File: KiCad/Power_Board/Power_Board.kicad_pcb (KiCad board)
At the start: 4 copper layers, 101.6 x 63.5 mm, 271 parts, among them P1 CONN_LEFT_TOP, P10 CONN_02X01, P2 CONN_RIGHT_TOP, P3 CONN_LEFT_BOTTOM, P4 CONN_RIGHT_BOTTOM, P5 CONN_02X01, P6 CONN_02X01, P7 CONN_02X01, P8 CONN_02X01, P9 CONN_02X01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

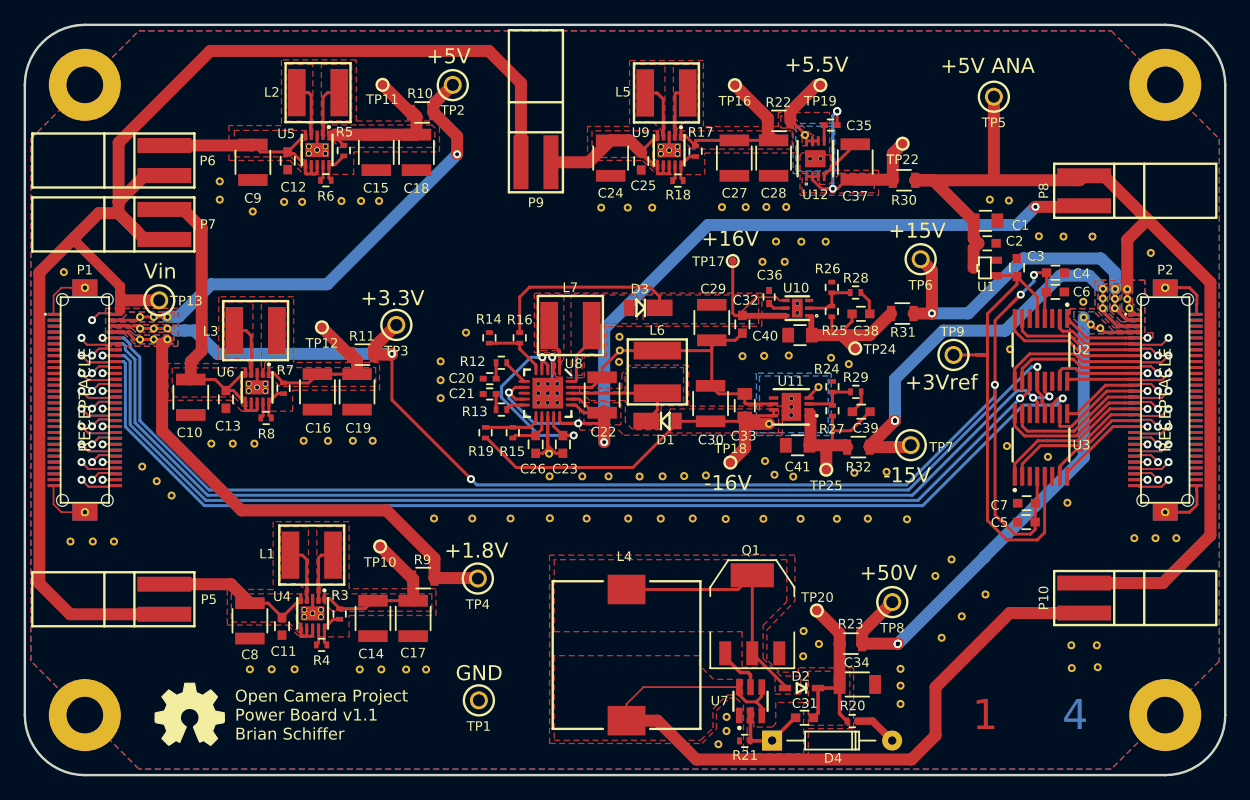
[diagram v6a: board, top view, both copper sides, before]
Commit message: More Cleanup
-Moved some traces away from the inductors to help with ground plane
continuity
-Increased via size in power traces
-Labeled power jumpers
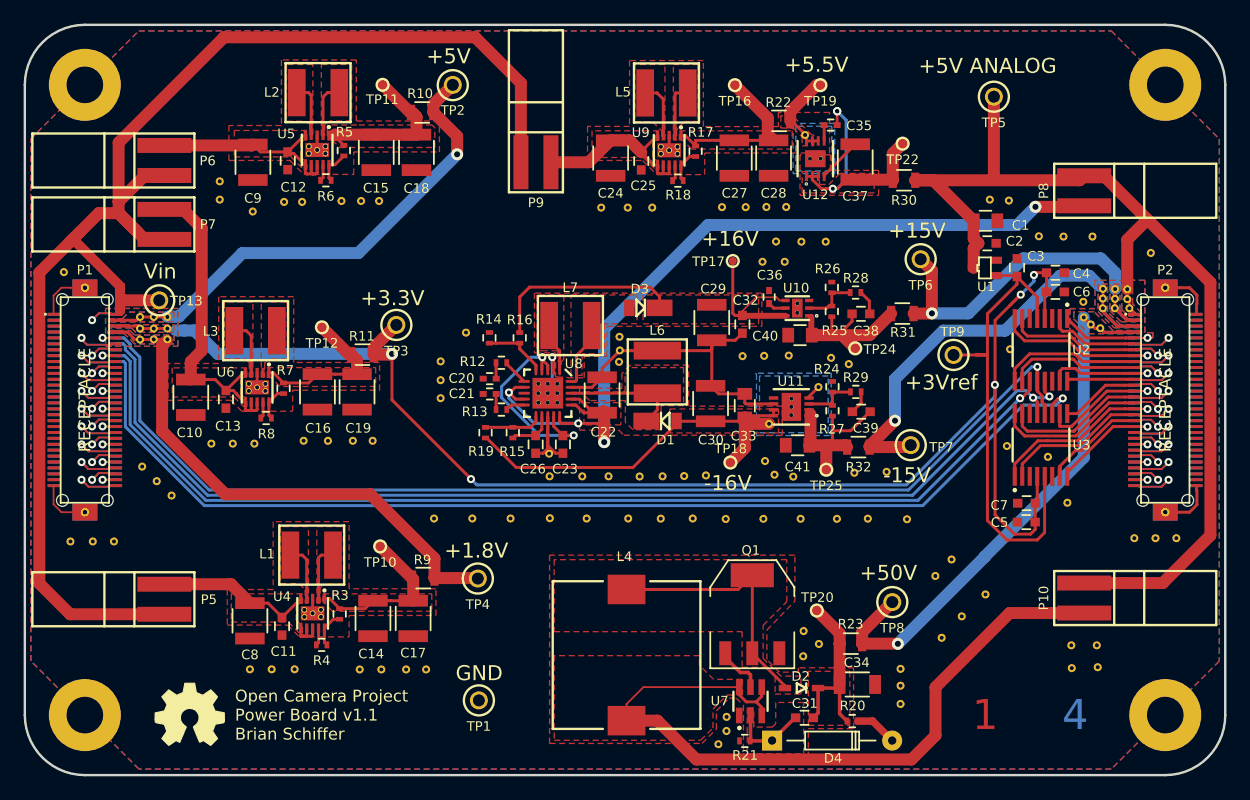
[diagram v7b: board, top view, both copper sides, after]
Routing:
- net /connectors/L1: track 150.5 -> 151.5 mm
- net Net-(C35-Pad1): track 26.8 -> 27.6 mm
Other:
- board text added: "+/-15V ENABLE"
- board text added: "+1.8V ENABLE"
- board text added: "+3.3V ENABLE"
- board text added: "+50V ENABLE"
- board text added: "+5V ANALOG"
- board text added: "+5V ANALOG ENABLE"
- board text added: "+5V ENABLE"
- board text removed: "+5V ANA"

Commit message: Added more ground vias around SPI lines.
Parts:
- added ?: , OpenCamera:STITCH_VIA, F.Cu at (104.4, 117.7)
- added ?: , OpenCamera:STITCH_VIA, F.Cu at (109.1, 114.5)
- added ?: , OpenCamera:STITCH_VIA, F.Cu at (111.7, 114.5)
- added ?: , OpenCamera:STITCH_VIA, F.Cu at (114.3, 114.5)
- added ?: , OpenCamera:STITCH_VIA, F.Cu at (117.0, 114.5)
- added ?: , OpenCamera:STITCH_VIA, F.Cu at (119.5, 114.5)
- added ?: , OpenCamera:STITCH_VIA, F.Cu at (122.1, 114.5)
- added ?: , OpenCamera:STITCH_VIA, F.Cu at (124.6, 114.5)
- added ?: , OpenCamera:STITCH_VIA, F.Cu at (127.6, 114.4)
- added ?: , OpenCamera:STITCH_VIA, F.Cu at (129.5, 114.4)
- added ?: , OpenCamera:STITCH_VIA, F.Cu at (131.4, 114.4)
- added ?: , OpenCamera:STITCH_VIA, F.Cu at (102.6, 117.2)
- added ?: , OpenCamera:STITCH_VIA, F.Cu at (106.6, 117.7)
- added ?: , OpenCamera:STITCH_VIA, F.Cu at (109.1, 117.7)
- added ?: , OpenCamera:STITCH_VIA, F.Cu at (111.8, 117.6)
- added ?: , OpenCamera:STITCH_VIA, F.Cu at (114.3, 117.7)
- added ?: , OpenCamera:STITCH_VIA, F.Cu at (117.0, 117.7)
- added ?: , OpenCamera:STITCH_VIA, F.Cu at (105.6, 113.2)
- added ?: , OpenCamera:STITCH_VIA, F.Cu at (106.8, 114.5)
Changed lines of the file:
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@@
 (kicad_pcb (version 4) (host pcbnew "(2015-04-19 BZR 5613)-product")
   (general
-    (links 644)
-    (no_connects 296)
-    (area 88.798399 76.098399 190.601601 139.801601)
+    (links 663)
+    (no_connects 0)
+    (area 83.190267 68.4732 202.615715 140.85886)
     (thickness 1.6)
     (drawings 34)
     (tracks 1453)
     (zones 0)
-    (modules 271)
+    (modules 290)
     (nets 116)
   )
@@
   )
   (module OpenCamera:STITCH_VIA (layer F.Cu)
+    (at 104.4067 117.729)
+    (fp_text reference "" (at 0 0.5) (layer Eco2.User) hide
+      (effects (font (size 0.8128 0.8128) (thickness 0.127)))
+    )
+    (fp_text value "" (at 0 -0.5) (layer Eco2.User) hide
+      (effects (font (size 1 1) (thickness 0.15)))
+    )
+    (pad "" thru_hole circle (at 0 0) (size 0.6858 0.6858) (drill 0.3302) (layers *.Cu)
+      (net 113 GND))
+  )
+  (module OpenCamera:STITCH_VIA (layer F.Cu)
+    (at 102.5652 117.1702)
+    (fp_text reference "" (at 0 0.5) (layer Eco2.User) hide
+      (effects (font (size 0.8128 0.8128) (thickness 0.127)))
+    )
+    (fp_text value "" (at 0 -0.5) (layer Eco2.User) hide
+      (effects (font (size 1 1) (thickness 0.15)))
+    )
+    (pad "" thru_hole circle (at 0 0) (size 0.6858 0.6858) (drill 0.3302) (layers *.Cu)
+      (net 113 GND))
+  )
+  (module OpenCamera:STITCH_VIA (layer F.Cu)
+    (at 106.553 117.7163)
+    (fp_text reference "" (at 0 0.5) (layer Eco2.User) hide
+      (effects (font (size 0.8128 0.8128) (thickness 0.127)))
+    )
+    (fp_text value "" (at 0 -0.5) (layer Eco2.User) hide
+      (effects (font (size 1 1) (thickness 0.15)))
+    )
+    (pad "" thru_hole circle (at 0 0) (size 0.6858 0.6858) (drill 0.3302) (layers *.Cu)
+      (net 113 GND))
+  )
+  (module OpenCamera:STITCH_VIA (layer F.Cu)
+    (at 109.1184 117.7163)
+    (fp_text reference "" (at 0 0.5) (layer Eco2.User) hide
+      (effects (font (size 0.8128 0.8128) (thickness 0.127)))
+    )
+    (fp_text value "" (at 0 -0.5) (layer Eco2.User) hide
+      (effects (font (size 1 1) (thickness 0.15)))
+    )
+    (pad "" thru_hole circle (at 0 0) (size 0.6858 0.6858) (drill 0.3302) (layers *.Cu)
+      (net 113 GND))
+  )
+  (module OpenCamera:STITCH_VIA (layer F.Cu)
+    (at 111.8362 117.6401)
+    (fp_text reference "" (at 0 0.5) (layer Eco2.User) hide
+      (effects (font (size 0.8128 0.8128) (thickness 0.127)))
+    )
+    (fp_text value "" (at 0 -0.5) (layer Eco2.User) hide
+      (effects (font (size 1 1) (thickness 0.15)))
+    )
+    (pad "" thru_hole circle (at 0 0) (size 0.6858 0.6858) (drill 0.3302) (layers *.Cu)
+      (net 113 GND))
+  )
+  (module OpenCamera:STITCH_VIA (layer F.Cu)
+    (at 114.3 117.6528)
+    (fp_text reference "" (at 0 0.5) (layer Eco2.User) hide
+      (effects (font (size 0.8128 0.8128) (thickness 0.127)))
+    )
+    (fp_text value "" (at 0 -0.5) (layer Eco2.User) hide
+      (effects (font (size 1 1) (thickness 0.15)))
+    )
+    (pad "" thru_hole circle (at 0 0) (size 0.6858 0.6858) (drill 0.3302) (layers *.Cu)
+      (net 113 GND))
+  )
+  (module OpenCamera:STITCH_VIA (layer F.Cu)
+    (at 117.0178 117.6528)
+    (fp_text reference "" (at 0 0.5) (layer Eco2.User) hide
+      (effects (font (size 0.8128 0.8128) (thickness 0.127)))
+    )
+    (fp_text value "" (at 0 -0.5) (layer Eco2.User) hide
+      (effects (font (size 1 1) (thickness 0.15)))
+    )
+    (pad "" thru_hole circle (at 0 0) (size 0.6858 0.6858) (drill 0.3302) (layers *.Cu)
+      (net 113 GND))
+  )
+  (module OpenCamera:STITCH_VIA (layer F.Cu)
+    (at 105.6386 113.157)
+    (fp_text reference "" (at 0 0.5) (layer Eco2.User) hide
+      (effects (font (size 0.8128 0.8128) (thickness 0.127)))
+    )
+    (fp_text value "" (at 0 -0.5) (layer Eco2.User) hide
+      (effects (font (size 1 1) (thickness 0.15)))
+    )
+    (pad "" thru_hole circle (at 0 0) (size 0.6858 0.6858) (drill 0.3302) (layers *.Cu)
+      (net 113 GND))
+  )
+  (module OpenCamera:STITCH_VIA (layer F.Cu)
+    (at 106.7943 114.4905)
+    (fp_text reference "" (at 0 0.5) (layer Eco2.User) hide
+      (effects (font (size 0.8128 0.8128) (thickness 0.127)))
+    )
+    (fp_text value "" (at 0 -0.5) (layer Eco2.User) hide
+      (effects (font (size 1 1) (thickness 0.15)))
+    )
+    (pad "" thru_hole circle (at 0 0) (size 0.6858 0.6858) (drill 0.3302) (layers *.Cu)
+      (net 113 GND))
+  )
+  (module OpenCamera:STITCH_VIA (layer F.Cu)
+    (at 109.1438 114.4905)
+    (fp_text reference "" (at 0 0.5) (layer Eco2.User) hide
+      (effects (font (size 0.8128 0.8128) (thickness 0.127)))
+    )
+    (fp_text value "" (at 0 -0.5) (layer Eco2.User) hide
+      (effects (font (size 1 1) (thickness 0.15)))
+    )
+    (pad "" thru_hole circle (at 0 0) (size 0.6858 0.6858) (drill 0.3302) (layers *.Cu)
+      (net 113 GND))
+  )
+  (module OpenCamera:STITCH_VIA (layer F.Cu)
+    (at 111.7219 114.4905)
+    (fp_text reference "" (at 0 0.5) (layer Eco2.User) hide
+      (effects (font (size 0.8128 0.8128) (thickness 0.127)))
+    )
+    (fp_text value "" (at 0 -0.5) (layer Eco2.User) hide
+      (effects (font (size 1 1) (thickness 0.15)))
+    )
+    (pad "" thru_hole circle (at 0 0) (size 0.6858 0.6858) (drill 0.3302) (layers *.Cu)
+      (net 113 GND))
+  )
+  (module OpenCamera:STITCH_VIA (layer F.Cu)
+    (at 114.2746 114.4905)
+    (fp_text reference "" (at 0 0.5) (layer Eco2.User) hide
+      (effects (font (size 0.8128 0.8128) (thickness 0.127)))
+    )
+    (fp_text value "" (at 0 -0.5) (layer Eco2.User) hide
+      (effects (font (size 1 1) (thickness 0.15)))
+    )
+    (pad "" thru_hole circle (at 0 0) (size 0.6858 0.6858) (drill 0.3302) (layers *.Cu)
+      (net 113 GND))
+  )
+  (module OpenCamera:STITCH_VIA (layer F.Cu)
+    (at 117.0051 114.4905)
+    (fp_text reference "" (at 0 0.5) (layer Eco2.User) hide
+      (effects (font (size 0.8128 0.8128) (thickness 0.127)))
+    )
+    (fp_text value "" (at 0 -0.5) (layer Eco2.User) hide
+      (effects (font (size 1 1) (thickness 0.15)))
+    )
+    (pad "" thru_hole circle (at 0 0) (size 0.6858 0.6858) (drill 0.3302) (layers *.Cu)
+      (net 113 GND))
+  )
+  (module OpenCamera:STITCH_VIA (layer F.Cu)
+    (at 119.5324 114.5032)
+    (fp_text reference "" (at 0 0.5) (layer Eco2.User) hide
+      (effects (font (size 0.8128 0.8128) (thickness 0.127)))
+    )
+    (fp_text value "" (at 0 -0.5) (layer Eco2.User) hide
+      (effects (font (size 1 1) (thickness 0.15)))
+    )
+    (pad "" thru_hole circle (at 0 0) (size 0.6858 0.6858) (drill 0.3302) (layers *.Cu)
+      (net 113 GND))
+  )
+  (module OpenCamera:STITCH_VIA (layer F.Cu)
+    (at 122.0851 114.4778)
+    (fp_text reference "" (at 0 0.5) (layer Eco2.User) hide
+      (effects (font (size 0.8128 0.8128) (thickness 0.127)))
+    )
+    (fp_text value "" (at 0 -0.5) (layer Eco2.User) hide
+      (effects (font (size 1 1) (thickness 0.15)))
+    )
+    (pad "" thru_hole circle (at 0 0) (size 0.6858 0.6858) (drill 0.3302) (layers *.Cu)
+      (net 113 GND))
+  )
+  (module OpenCamera:STITCH_VIA (layer F.Cu)
+    (at 124.5616 114.4651)
+    (fp_text reference "" (at 0 0.5) (layer Eco2.User) hide
+      (effects (font (size 0.8128 0.8128) (thickness 0.127)))
+    )
+    (fp_text value "" (at 0 -0.5) (layer Eco2.User) hide
+      (effects (font (size 1 1) (thickness 0.15)))
+    )
+    (pad "" thru_hole circle (at 0 0) (size 0.6858 0.6858) (drill 0.3302) (layers *.Cu)
+      (net 113 GND))
+  )
+  (module OpenCamera:STITCH_VIA (layer F.Cu)
+    (at 127.5842 114.4397)
+    (fp_text reference "" (at 0 0.5) (layer Eco2.User) hide
+      (effects (font (size 0.8128 0.8128) (thickness 0.127)))
+    )
+    (fp_text value "" (at 0 -0.5) (layer Eco2.User) hide
+      (effects (font (size 1 1) (thickness 0.15)))
+    )
+    (pad "" thru_hole circle (at 0 0) (size 0.6858 0.6858) (drill 0.3302) (layers *.Cu)
+      (net 113 GND))
+  )
+  (module OpenCamera:STITCH_VIA (layer F.Cu)
+    (at 129.4511 114.4143)
+    (fp_text reference "" (at 0 0.5) (layer Eco2.User) hide
+      (effects (font (size 0.8128 0.8128) (thickness 0.127)))
+    )
+    (fp_text value "" (at 0 -0.5) (layer Eco2.User) hide
+      (effects (font (size 1 1) (thickness 0.15)))
+    )
+    (pad "" thru_hole circle (at 0 0) (size 0.6858 0.6858) (drill 0.3302) (layers *.Cu)
+      (net 113 GND))
+  )
+  (module OpenCamera:STITCH_VIA (layer F.Cu)
+    (at 131.3815 114.4143)
+    (fp_text reference "" (at 0 0.5) (layer Eco2.User) hide
+      (effects (font (size 0.8128 0.8128) (thickness 0.127)))
+    )
+    (fp_text value "" (at 0 -0.5) (layer Eco2.User) hide
+      (effects (font (size 1 1) (thickness 0.15)))
+    )
+    (pad "" thru_hole circle (at 0 0) (size 0.6858 0.6858) (drill 0.3302) (layers *.Cu)
+      (net 113 GND))
+  )
+  (module OpenCamera:STITCH_VIA (layer F.Cu)
     (at 172.1866 91.0717)
     (fp_text reference "" (at 0 0.5) (layer Eco2.User) hide
@@
   (segment (start 118.4051 104.0146) (end 120.1872 101.7524) (width 0.254) (layer F.Cu) (net 56) (status 10))
   (segment (start 118.4051 104.1146) (end 118.4051 104.0146) (width 0.254) (layer F.Cu) (net 56) (status 30))
-  (via (at 119.9744 104.0511) (size 1.016) (drill 0.508) (layers F.Cu B.Cu) (net 56) (status 1000000))
+  (via (at 119.9744 104.0511) (size 1.016) (drill 0.508) (layers F.Cu B.Cu) (net 56))
   (segment (start 118.4051 104.1146) (end 119.9109 104.1146) (width 0.254) (layer F.Cu) (net 56) (status 10))
   (via (at 173.1899 99.0346) (size 0.6858) (drill 0.3302) (layers F.Cu B.Cu) (net 56))
